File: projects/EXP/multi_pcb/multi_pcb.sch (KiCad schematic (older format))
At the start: 8 parts, among them J1 Conn_01x02, J2 Conn_01x02, J3 Conn_01x02, J4 Conn_01x02, SW1 SW_SPST, SW2 SW_SPST

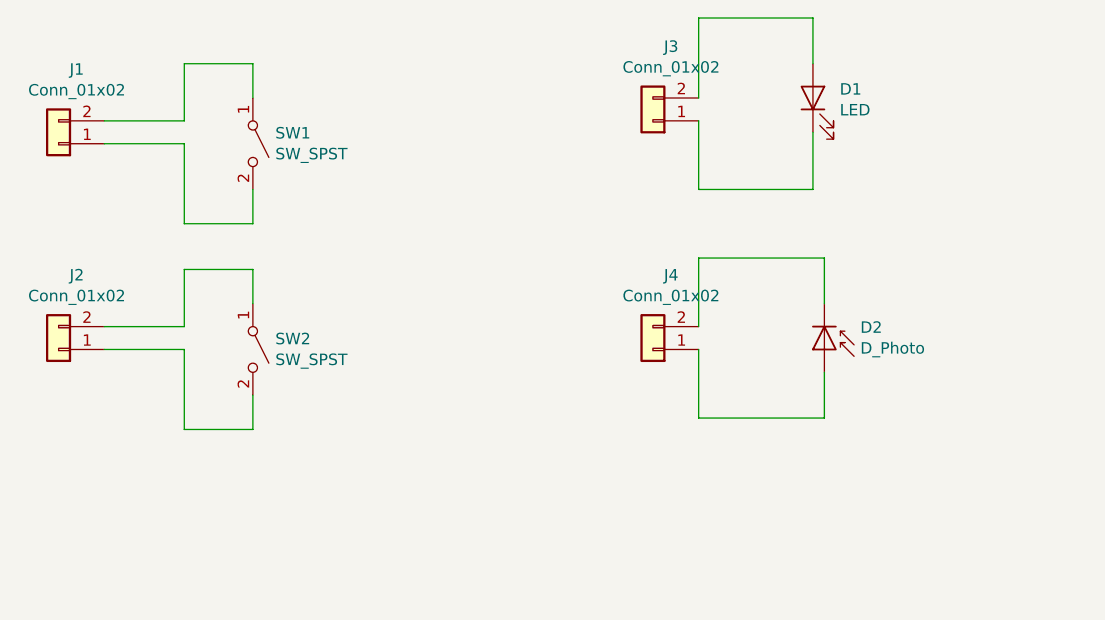
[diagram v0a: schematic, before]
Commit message: New library files and schematics with ESE31 and DT045 switches
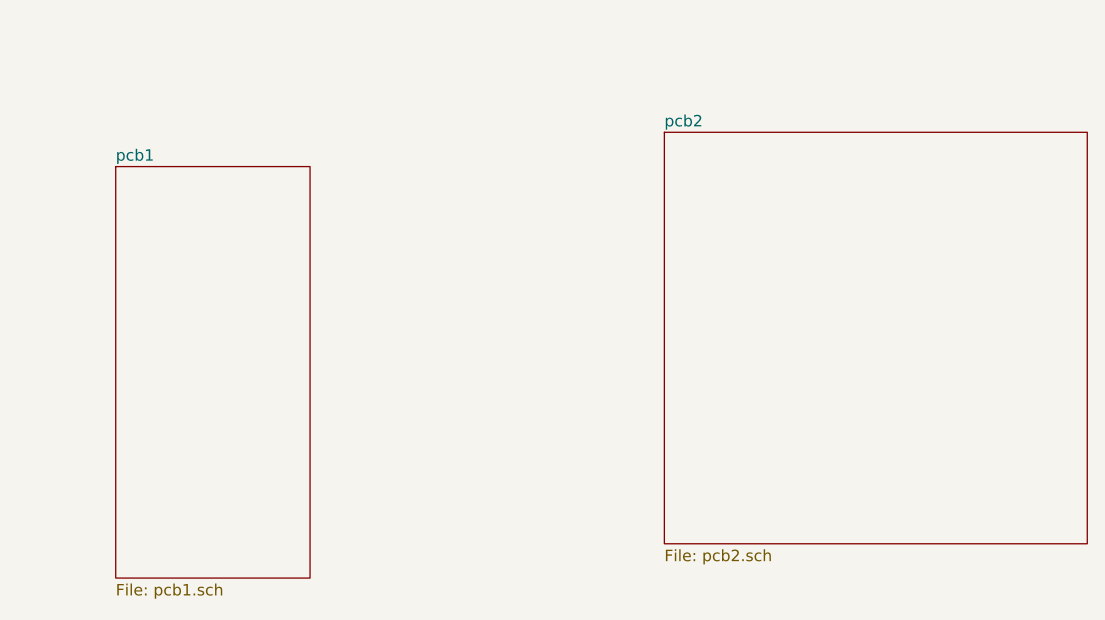
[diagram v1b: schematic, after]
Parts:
- removed D1: LED, LED_SMD:LED_0805_2012Metric, symbol Device:LED
- removed D2: D_Photo, LED_SMD:LED_0805_2012Metric, symbol Device:D_Photo
- removed J1, J2, J3, J4: Conn_01x02, Connector_JST:JST_EH_B02B-EH-A_1x02_P2.50mm_Vertical, symbol Connector_Generic:Conn_01x02
- removed SW1, SW2: SW_SPST, Button_Switch_SMD:SW_DIP_SPSTx01_Slide_6.7x4.1mm_W6.73mm_P2.54mm_LowProfile_JPin, symbol Switch:SW_SPST
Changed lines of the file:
@@
 EESchema Schematic File Version 4
+LIBS:multi_pcb-cache
+LIBS:pcb1-cache
+LIBS:pcb2-cache
 EELAYER 26 0
 EELAYER END
 $Descr A4 11693 8268
 encoding utf-8
-Sheet 1 1
+Sheet 1 3
 Title ""
 Date ""
@@
 Comment4 ""
 $EndDescr
-$Comp
-L Connector_Generic:Conn_01x02 J1
-U 1 1 5CC02A54
-P 2500 2300
-F 0 "J1" H 2420 1975 50  0000 C CNN
-F 1 "Conn_01x02" H 2420 2066 50  0000 C CNN
-F 2 "Connector_JST:JST_EH_B02B-EH-A_1x02_P2.50mm_Vertical" H 2500 2300 50  0001 C CNN
-F 3 "~" H 2500 2300 50  0001 C CNN
-	1    2500 2300
-	-1   0    0    1
-$EndComp
-$Comp
-L Switch:SW_SPST SW1
-U 1 1 5CC02D08
-P 3350 2300
-F 0 "SW1" V 3304 2398 50  0000 L CNN
-F 1 "SW_SPST" V 3395 2398 50  0000 L CNN
-F 2 "Button_Switch_SMD:SW_DIP_SPSTx01_Slide_6.7x4.1mm_W6.73mm_P2.54mm_LowProfile_JPin" H 3350 2300 50  0001 C CNN
-F 3 "" H 3350 2300 50  0001 C CNN
-	1    3350 2300
-	0    1    1    0
-$EndComp
-Wire Wire Line
-	2700 2200 3050 2200
-Wire Wire Line
-	3050 2200 3050 1950
-Wire Wire Line
-	3050 1950 3350 1950
-Wire Wire Line
-	3350 1950 3350 2100
-Wire Wire Line
-	2700 2300 3050 2300
-Wire Wire Line
-	3050 2300 3050 2650
-Wire Wire Line
-	3050 2650 3350 2650
-Wire Wire Line
-	3350 2650 3350 2500
-$Comp
-L Connector_Generic:Conn_01x02 J2
-U 1 1 5CC02EF3
-P 2500 3200
-F 0 "J2" H 2420 2875 50  0000 C CNN
-F 1 "Conn_01x02" H 2420 2966 50  0000 C CNN
-F 2 "Connector_JST:JST_EH_B02B-EH-A_1x02_P2.50mm_Vertical" H 2500 3200 50  0001 C CNN
-F 3 "~" H 2500 3200 50  0001 C CNN
-	1    2500 3200
-	-1   0    0    1
-$EndComp
-$Comp
-L Switch:SW_SPST SW2
-U 1 1 5CC02EFA
-P 3350 3200
-F 0 "SW2" V 3304 3298 50  0000 L CNN
-F 1 "SW_SPST" V 3395 3298 50  0000 L CNN
-F 2 "Button_Switch_SMD:SW_DIP_SPSTx01_Slide_6.7x4.1mm_W6.73mm_P2.54mm_LowProfile_JPin" H 3350 3200 50  0001 C CNN
-F 3 "" H 3350 3200 50  0001 C CNN
-	1    3350 3200
-	0    1    1    0
-$EndComp
-Wire Wire Line
-	2700 3100 3050 3100
-Wire Wire Line
-	3050 3100 3050 2850
-Wire Wire Line
-	3050 2850 3350 2850
-Wire Wire Line
-	3350 2850 3350 3000
-Wire Wire Line
-	2700 3200 3050 3200
-Wire Wire Line
-	3050 3200 3050 3550
-Wire Wire Line
-	3050 3550 3350 3550
-Wire Wire Line
-	3350 3550 3350 3400
-$Comp
-L Connector_Generic:Conn_01x02 J3
-U 1 1 5CC0302A
-P 5100 2200
-F 0 "J3" H 5020 1875 50  0000 C CNN
-F 1 "Conn_01x02" H 5020 1966 50  0000 C CNN
-F 2 "Connector_JST:JST_EH_B02B-EH-A_1x02_P2.50mm_Vertical" H 5100 2200 50  0001 C CNN
-F 3 "~" H 5100 2200 50  0001 C CNN
-	1    5100 2200
-	-1   0    0    1
-$EndComp
-$Comp
-L Device:LED D1
-U 1 1 5CC030D0
-P 5800 2100
-F 0 "D1" V 5838 1983 50  0000 R CNN
-F 1 "LED" V 5747 1983 50  0000 R CNN
-F 2 "LED_SMD:LED_0805_2012Metric" H 5800 2100 50  0001 C CNN
-F 3 "~" H 5800 2100 50  0001 C CNN
-	1    5800 2100
-	0    -1   -1   0
-$EndComp
-$Comp
-L Connector_Generic:Conn_01x02 J4
-U 1 1 5CC03252
-P 5100 3200
-F 0 "J4" H 5020 2875 50  0000 C CNN
-F 1 "Conn_01x02" H 5020 2966 50  0000 C CNN
-F 2 "Connector_JST:JST_EH_B02B-EH-A_1x02_P2.50mm_Vertical" H 5100 3200 50  0001 C CNN
-F 3 "~" H 5100 3200 50  0001 C CNN
-	1    5100 3200
-	-1   0    0    1
-$EndComp
-$Comp
-L Device:D_Photo D2
-U 1 1 5CC03301
-P 5850 3200
-F 0 "D2" V 5754 3357 50  0000 L CNN
-F 1 "D_Photo" V 5845 3357 50  0000 L CNN
-F 2 "LED_SMD:LED_0805_2012Metric" H 5800 3200 50  0001 C CNN
-F 3 "~" H 5800 3200 50  0001 C CNN
-	1    5850 3200
-	0    1    1    0
-$EndComp
-Wire Wire Line
-	5300 3100 5300 2800
-Wire Wire Line
-	5300 2800 5850 2800
-Wire Wire Line
-	5850 2800 5850 3000
-Wire Wire Line
-	5850 3300 5850 3500
-Wire Wire Line
-	5850 3500 5300 3500
-Wire Wire Line
-	5300 3500 5300 3200
-Wire Wire Line
-	5300 2100 5300 1750
-Wire Wire Line
-	5300 1750 5800 1750
-Wire Wire Line
-	5800 1750 5800 1950
-Wire Wire Line
-	5800 2250 5800 2500
-Wire Wire Line
-	5800 2500 5300 2500
-Wire Wire Line
-	5300 2500 5300 2200
+$Sheet
+S 2750 2400 850  1800
+U 5CCAD6CF
+F0 "pcb1" 50
+F1 "pcb1.sch" 50
+$EndSheet
+$Sheet
+S 5150 2250 1850 1800
+U 5CCAD6D2
+F0 "pcb2" 50
+F1 "pcb2.sch" 50
+$EndSheet
 $EndSCHEMATC
